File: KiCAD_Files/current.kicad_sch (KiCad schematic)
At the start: 14 parts, among them U5 AMC1301DWR, U8 MCP6486UT-E/LT

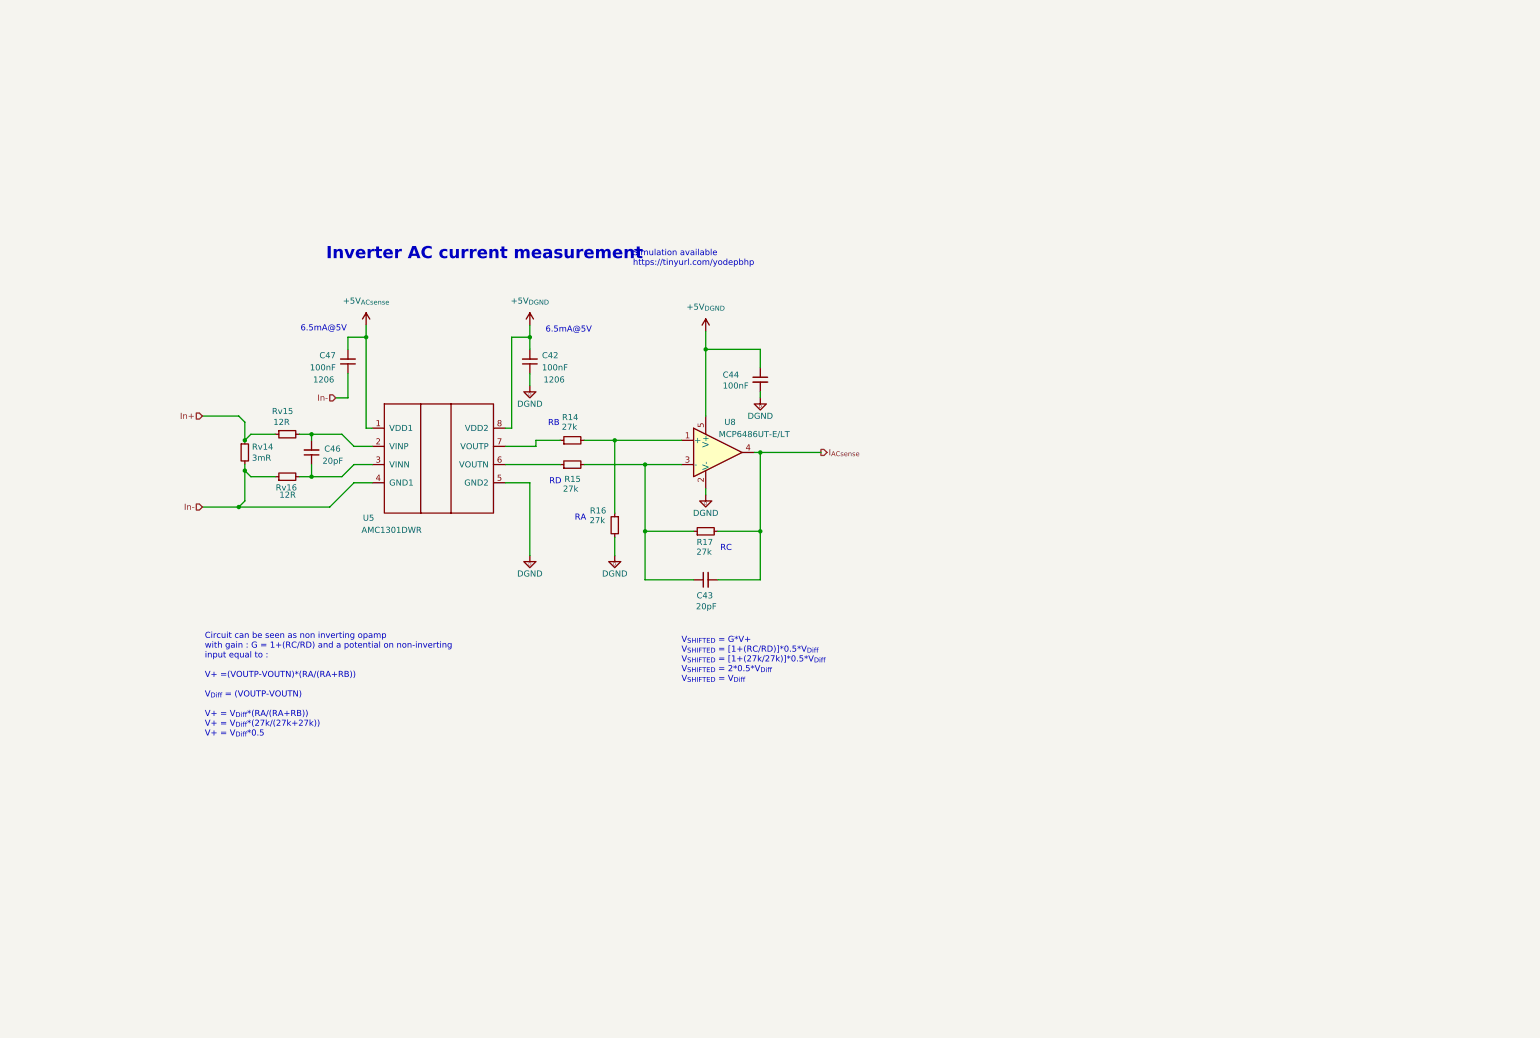
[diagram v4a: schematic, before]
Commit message: Added passive references. Added ESD protection for MCU pins.
Signed-off-by: Jean Alinei <jean.alinei@owntech.org>
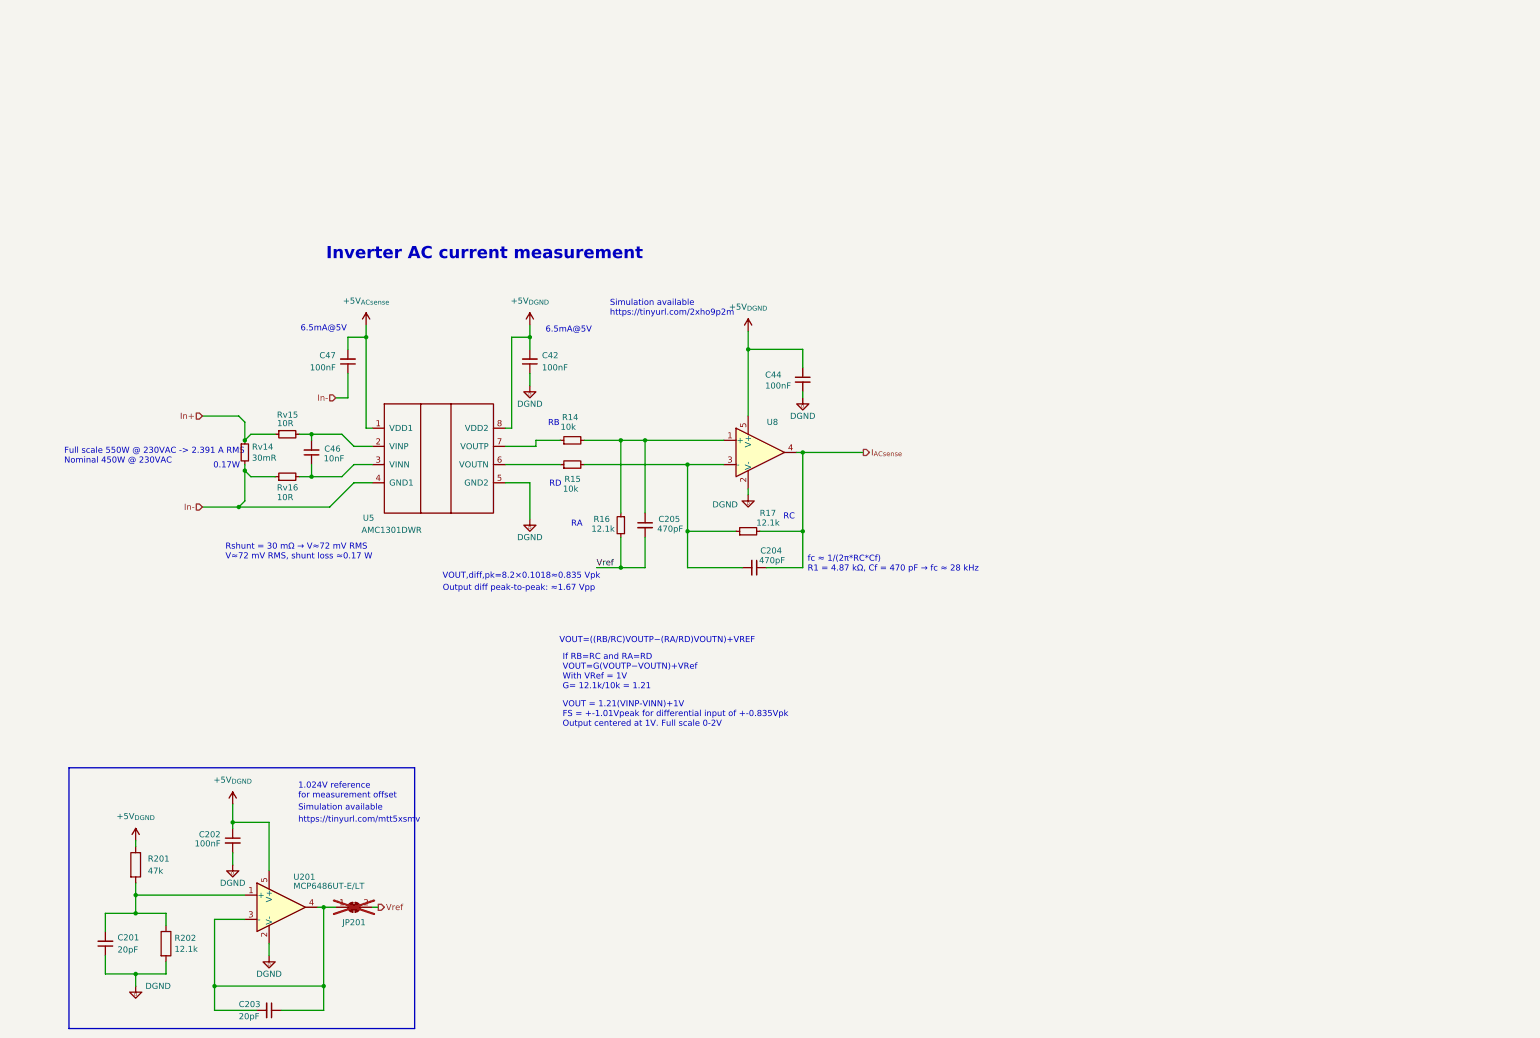
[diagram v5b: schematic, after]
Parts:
- removed C43: 20pF, Footprints:C_0805_2012Metric, symbol Device:C_Small
- added C201, C203: 20pF, Footprints:C_0805_2012Metric, symbol Device:C_Small
- added C202: 100nF, Capacitor_SMD:C_0805_2012Metric, symbol Device:C_Small
- added C204, C205: 470pF, Footprints:C_0805_2012Metric, symbol Device:C_Small
- added JP201: SolderJumper, Jumper:SolderJumper-2_P1.3mm_Bridged_RoundedPad1.0x1.5mm, symbol Jumper:SolderJumper_2_Bridged
- added R201: 47k, Footprints:R_0805_2012Metric, symbol Device:R
- added R202: 12.1k, Footprints:R_0805_2012Metric, symbol Device:R
- added U201: MCP6486UT-E/LT, Package_TO_SOT_SMD:SOT-353_SC-70-5_Handsoldering, symbol Amplifier_Operational:TLV6001DCK
- C42, C47: Dielectric X7R -> (none); LCSC C5449000 -> C24497; Metal content BaTiO3 -> (none); Package 1206 -> (none); Subfunction VIHigh measure -> (none); Voltage 50V -> (none); manf# C1206C104K5RAC7867 -> (none)
- C44: Dielectric X7R -> (none); LCSC C5449000 -> C49678; Package 1206 -> (none); Voltage 50V -> (none); manf# C1206C104K5RAC7867 -> (none)
- C46: value 20pF -> 10nF; Dielectric NP0 -> (none); LCSC (none) -> C1710; Package 0805 -> (none); Voltage 50V -> (none); manf# CC0805JRNPO9BN200 -> (none)
- R14, R15: value 27k -> 10k; LCSC (none) -> C17414; Package 0805 -> (none); Technology Thin film -> (none); manf# RT0805DRD0727KL -> (none)
- R16, R17: value 27k -> 12.1k; LCSC (none) -> C17431; Package 0805 -> (none); Technology Thin film -> (none); manf# RT0805DRD0727KL -> (none)
- Rv14: value 3mR -> 30mR; LCSC (none) -> C46634451
- Rv15, Rv16: value 12R -> 10R; LCSC (none) -> C17415
- U8: Rotation Offset (none) -> 90; Subfunction IILow Measure -> (none); manf# MCP6486UT-E/LT -> (none)
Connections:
- net +5V_{DGND}: now also C202.1, R201.1, U201.5 (V+)
- net DGND: now also C201.1, C202.2, R202.2, U201.2 (V-); no longer R16.2
- net I_{ACsense}: now also C204.1
- net at R14.2, R16.1, U8.1 (+): now also C205.1
- net at R15.2, R17.1, U8.3 (-): now also C204.2
- new net: C203.1, C203.2, JP201.1 (A), U201.3 (-), U201.4
- new net: C201.2, R201.2, R202.1, U201.1 (+)
- new net Vref: C205.2, JP201.2 (B), R16.2
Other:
- note added: "0.17W"
- note added: "1.024V reference for measurement offset"
- note added: "Full scale 550W @ 230VAC -> 2.391 A RMS Nominal 450W @ 230VAC"
- note added: "If RB=RC and RA=RD VOUT​=G(VOUTP​−VOUTN​)+VRef With VRef = 1V G= 12.1k/10k = 1.21"
- note added: "Output diff peak-to-peak: ≈1.67 Vpp"
- note added: "Rshunt = 30 mΩ → V≈72 mV RMS V≈72 mV RMS, shunt loss ≈0.17 W"
- note added: "Simulation available"
- note added: "Simulation available https://tinyurl.com/2xho9p2m"
- note added: "VOUT = 1.21(VINP-VINN)+1V FS = +-1.01Vpeak for differential input of +-0.835Vpk Output centered at 1V. Full scale 0-2V"
- note added: "VOUT,diff,pk​=8.2×0.1018≈0.835 Vpk"
- note added: "VOUT​=((RB/RC)VOUTP​−(RA/RD)VOUTN​)+VREF​"
- note added: "fc ​≈ 1/(2π*RC*Cf)​ R1 = 4.87 kΩ, Cf = 470 pF → fc ≈ 28 kHz"
- note added: "https://tinyurl.com/mtt5xsmv"
- note removed: "Circuit can be seen as non inverting opamp with gain : G = 1+(RC/RD) and a potential on non-inverting input equal to : V+ =(VOUTP-VOUTN)*(RA/(RA+RB)) V_{Diff} = (VOUTP-VOUTN) V+ = V_{Diff}*(RA/(RA+RB)) V+ = V_{Diff}*(27k/(27k+27k)) V+ = V_{Diff}*0.5"
- note removed: "Simulation available https://tinyurl.com/yodepbhp"
- note removed: "V_{SHIFTED} = G*V+ V_{SHIFTED} = [1+(RC/RD)]*0.5*V_{Diff} V_{SHIFTED} = [1+(27k/27k)]*0.5*V_{Diff} V_{SHIFTED} = 2*0.5*V_{Diff} V_{SHIFTED} = V_{Diff}"
- moved on the sheet: C44, R16, R17, U8

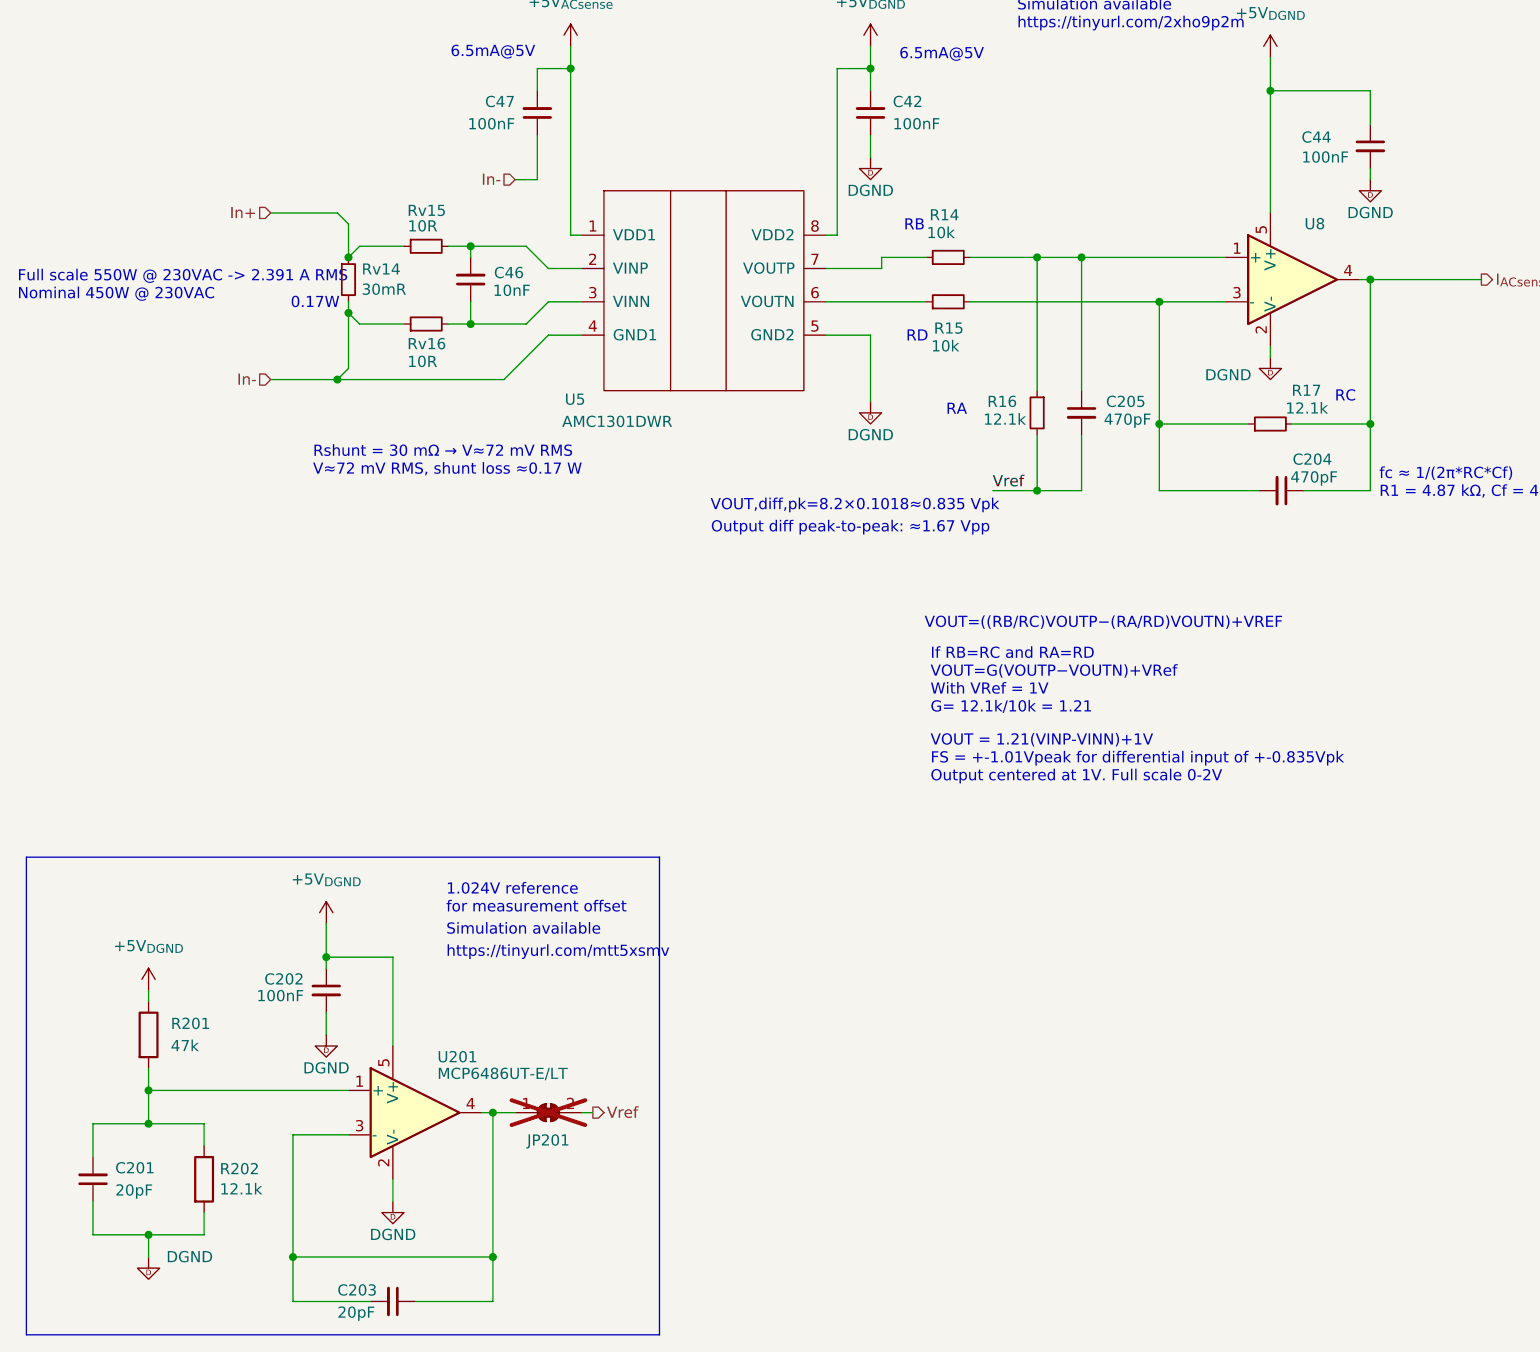
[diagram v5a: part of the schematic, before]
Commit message: Added TL431 for AC measurement 5V regulation. Added more film capacitance. Increased size of 100V ceramic caps to 1210.
Signed-off-by: Jean Alinei <jean.alinei@owntech.org>
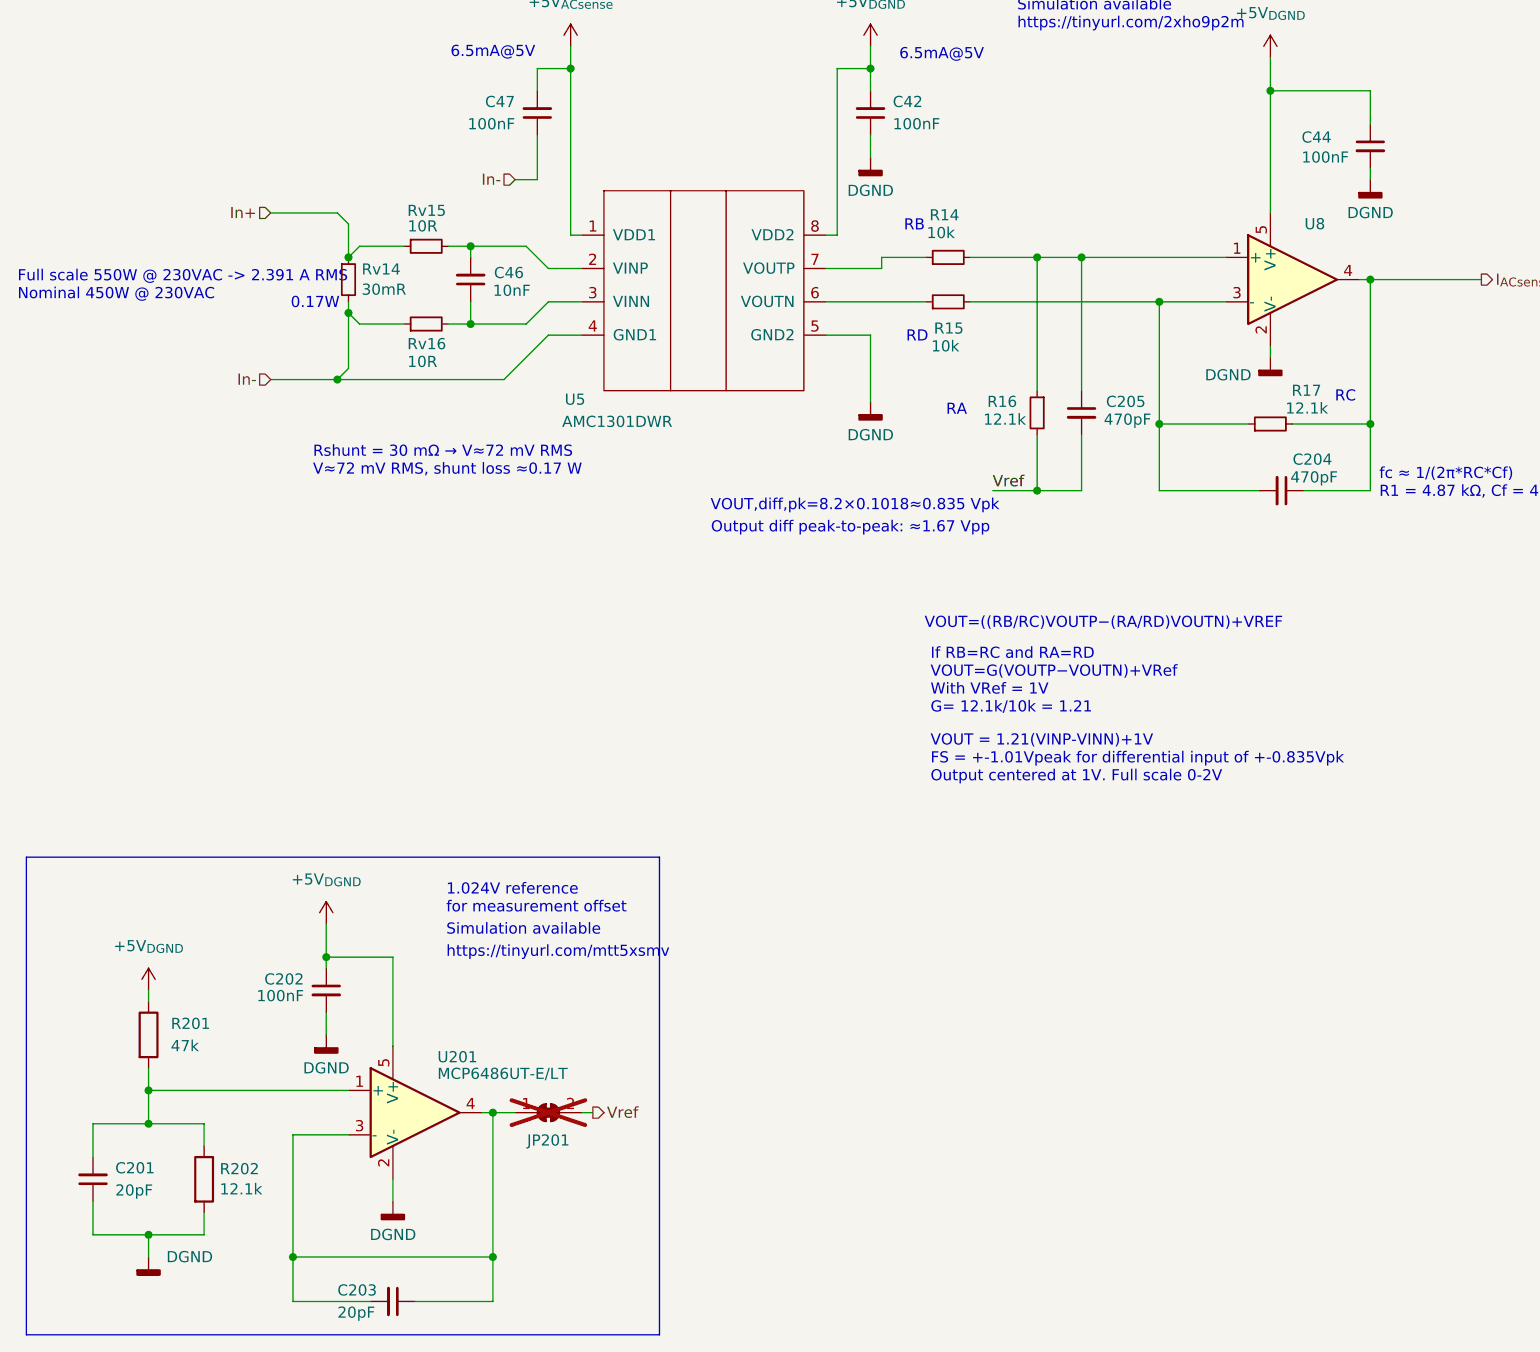
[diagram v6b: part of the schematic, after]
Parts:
- U201: footprint Package_TO_SOT_SMD:SOT-353_SC-70-5_Handsoldering -> Package_TO_SOT_SMD:SOT-353_SC-70-5
- U8: footprint Package_TO_SOT_SMD:SOT-353_SC-70-5_Handsoldering -> Package_TO_SOT_SMD:SOT-353_SC-70-5; symbol Symbols:MCP6486UT-E/LT -> Symbols:MCP6486UT-E/LT

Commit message: Tidied up the schematic. Added the pdf version for V0.9.
Signed-off-by: Jean Alinei <jean.alinei@owntech.org>
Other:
- title: Micro-inverter - 400W -> Grid current measurement
- moved on the sheet: C201, C202, C203, C204, C205, C42, C44, C46, C47, JP201, R14, R15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
